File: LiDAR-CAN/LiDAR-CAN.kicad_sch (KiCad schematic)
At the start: 0 parts

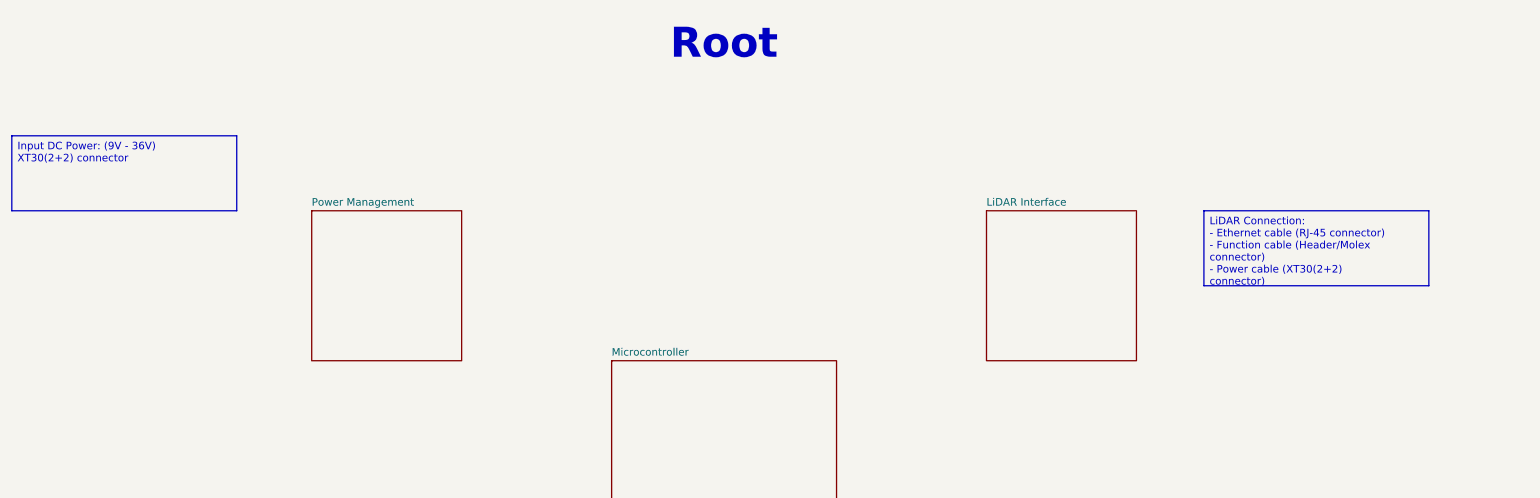
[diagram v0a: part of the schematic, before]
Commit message: Add LiDAR Interface complete circuit
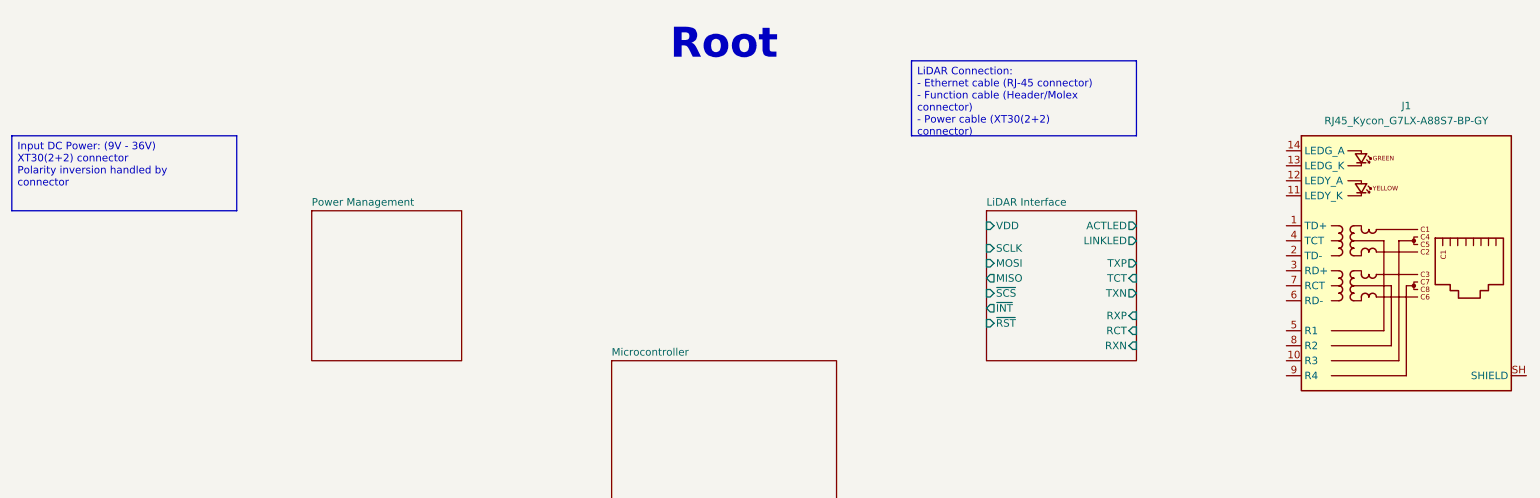
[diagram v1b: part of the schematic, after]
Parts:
- added J1: RJ45_Kycon_G7LX-A88S7-BP-GY, Connector_RJ:RJ45_Kycon_G7LX-A88S7-BP-xx_Horizontal, symbol Connector:RJ45_Kycon_G7LX-A88S7-BP-GY
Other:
- sheet LiDAR Interface ports: added ACTLED, LINKLED, MISO, MOSI, RCT, RXN, RXP, SCLK, TCT, TXN, TXP, VDD, ~{INT}, ~{RST}, ~{SCS}; removed none
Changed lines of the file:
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@@
 	(text_box "LiDAR Connection:\n- Ethernet cable (RJ-45 connector)\n- Function cable (Header/Molex connector)\n- Power cable (XT30(2+2) connector)"
 		(exclude_from_sim no)
-		(at 227.33 50.8 0)
+		(at 177.8 25.4 0)
 		(size 38.1 12.7)
 		(margins 0.9525 0.9525 0.9525 0.9525)
@@
 		)
 	)
-	(text_box "Input DC Power: (9V - 36V)\nXT30(2+2) connector"
+	(text_box "Input DC Power: (9V - 36V)\nXT30(2+2) connector\nPolarity inversion handled by connector"
 		(exclude_from_sim no)
 		(at 25.4 38.1 0)
@@
 		)
 	)
-	(sheet
-		(at 127 76.2)
-		(size 38.1 38.1)
+	(symbol
+		(lib_id "Connector:RJ45_Kycon_G7LX-A88S7-BP-GY")
+		(at 261.62 60.96 0)
+		(unit 1)
 		(exclude_from_sim no)
 		(in_bom yes)
@@
 		(dnp no)
 		(fields_autoplaced yes)
+		(property "Reference" "J1"
+			(at 261.62 33.02 0)
+			(effects
+				(font
+					(size 1.27 1.27)
+				)
+			)
+		)
+		(property "Value" "RJ45_Kycon_G7LX-A88S7-BP-GY"
+			(at 261.62 35.56 0)
+			(effects
+				(font
+					(size 1.27 1.27)
+				)
+			)
+		)
+		(property "Footprint" "Connector_RJ:RJ45_Kycon_G7LX-A88S7-BP-xx_Horizontal"
+			(at 261.62 33.02 0)
+			(effects
+				(font
+					(size 1.27 1.27)
+				)
+				(hide yes)
+			)
+		)
+		(property "Datasheet" "http://www.kycon.com/Pub_Eng_Draw/G7LX-A88S7-BP-GY.pdf"
+			(at 261.62 30.48 0)
+			(effects
+				(font
+					(size 1.27 1.27)
+				)
+				(hide yes)
+			)
+		)
+		(property "Description" "1 Port RJ45 Magjack Connector Through Hole 10/100 Base-T, AutoMDIX"
+			(at 261.62 60.96 0)
+			(effects
+				(font
+					(size 1.27 1.27)
+				)
+				(hide yes)
+			)
+		)
+		(pin "12"
+		)
+		(pin "2"
+		)
+		(pin "SH"
+		)
+		(pin "8"
+		)
+		(pin "6"
+		)
+		(pin "11"
+		)
+		(pin "9"
+		)
+		(pin "13"
+		)
+		(pin "5"
+		)
+		(pin "1"
+		)
+		(pin "14"
+		)
+		(pin "4"
+		)
+		(pin "3"
+		)
+		(pin "7"
+		)
+		(pin "10"
+		)
+		(instances
+			(project ""
+				(path "/56db6f21-0e4a-4321-bd8a-db37f1842dd9"
+					(reference "J1")
+					(unit 1)
+				)
+			)
+		)
+	)
+	(sheet
+		(at 127 76.2)
+		(size 38.1 38.1)
+		(exclude_from_sim no)
+		(in_bom yes)
+		(on_board yes)
+		(dnp no)
+		(fields_autoplaced yes)
 		(stroke
 			(width 0.1524)
@@
 			)
 		)
+		(pin "ACTLED" output
+			(at 215.9 53.34 0)
+			(effects
+				(font
+					(size 1.27 1.27)
+				)
+				(justify right)
+			)
+		)
+		(pin "LINKLED" output
+			(at 215.9 55.88 0)
+			(effects
+				(font
+					(size 1.27 1.27)
+				)
+				(justify right)
+			)
+		)
+		(pin "MISO" output
+			(at 190.5 62.23 180)
+			(effects
+				(font
+					(size 1.27 1.27)
+				)
+				(justify left)
+			)
+		)
+		(pin "MOSI" input
+			(at 190.5 59.69 180)
+			(effects
+				(font
+					(size 1.27 1.27)
+				)
+				(justify left)
+			)
+		)
+		(pin "RCT" input
+			(at 215.9 71.12 0)
+			(effects
+				(font
+					(size 1.27 1.27)
+				)
+				(justify right)
+			)
+		)
+		(pin "RXN" input
+			(at 215.9 73.66 0)
+			(effects
+				(font
+					(size 1.27 1.27)
+				)
+				(justify right)
+			)
+		)
+		(pin "RXP" input
+			(at 215.9 68.58 0)
+			(effects
+				(font
+					(size 1.27 1.27)
+				)
+				(justify right)
+			)
+		)
+		(pin "SCLK" input
+			(at 190.5 57.15 180)
+			(effects
+				(font
+					(size 1.27 1.27)
+				)
+				(justify left)
+			)
+		)
+		(pin "TCT" input
+			(at 215.9 62.23 0)
+			(effects
+				(font
+					(size 1.27 1.27)
+				)
+				(justify right)
+			)
+		)
+		(pin "TXN" output
+			(at 215.9 64.77 0)
+			(effects
+				(font
+					(size 1.27 1.27)
+				)
+				(justify right)
+			)
+		)
+		(pin "TXP" output
+			(at 215.9 59.69 0)
+			(effects
+				(font
+					(size 1.27 1.27)
+				)
+				(justify right)
+			)
+		)
+		(pin "VDD" input
+			(at 190.5 53.34 180)
+			(effects
+				(font
+					(size 1.27 1.27)
+				)
+				(justify left)
+			)
+		)
+		(pin "~{INT}" output
+			(at 190.5 67.31 180)
+			(effects
+				(font
+					(size 1.27 1.27)
+				)
+				(justify left)
+			)
+		)
+		(pin "~{RST}" input
+			(at 190.5 69.85 180)
+			(effects
+				(font
+					(size 1.27 1.27)
+				)
+				(justify left)
+			)
+		)
+		(pin "~{SCS}" input
+			(at 190.5 64.77 180)
+			(effects
+				(font
+					(size 1.27 1.27)
+				)
+				(justify left)
+			)
+		)

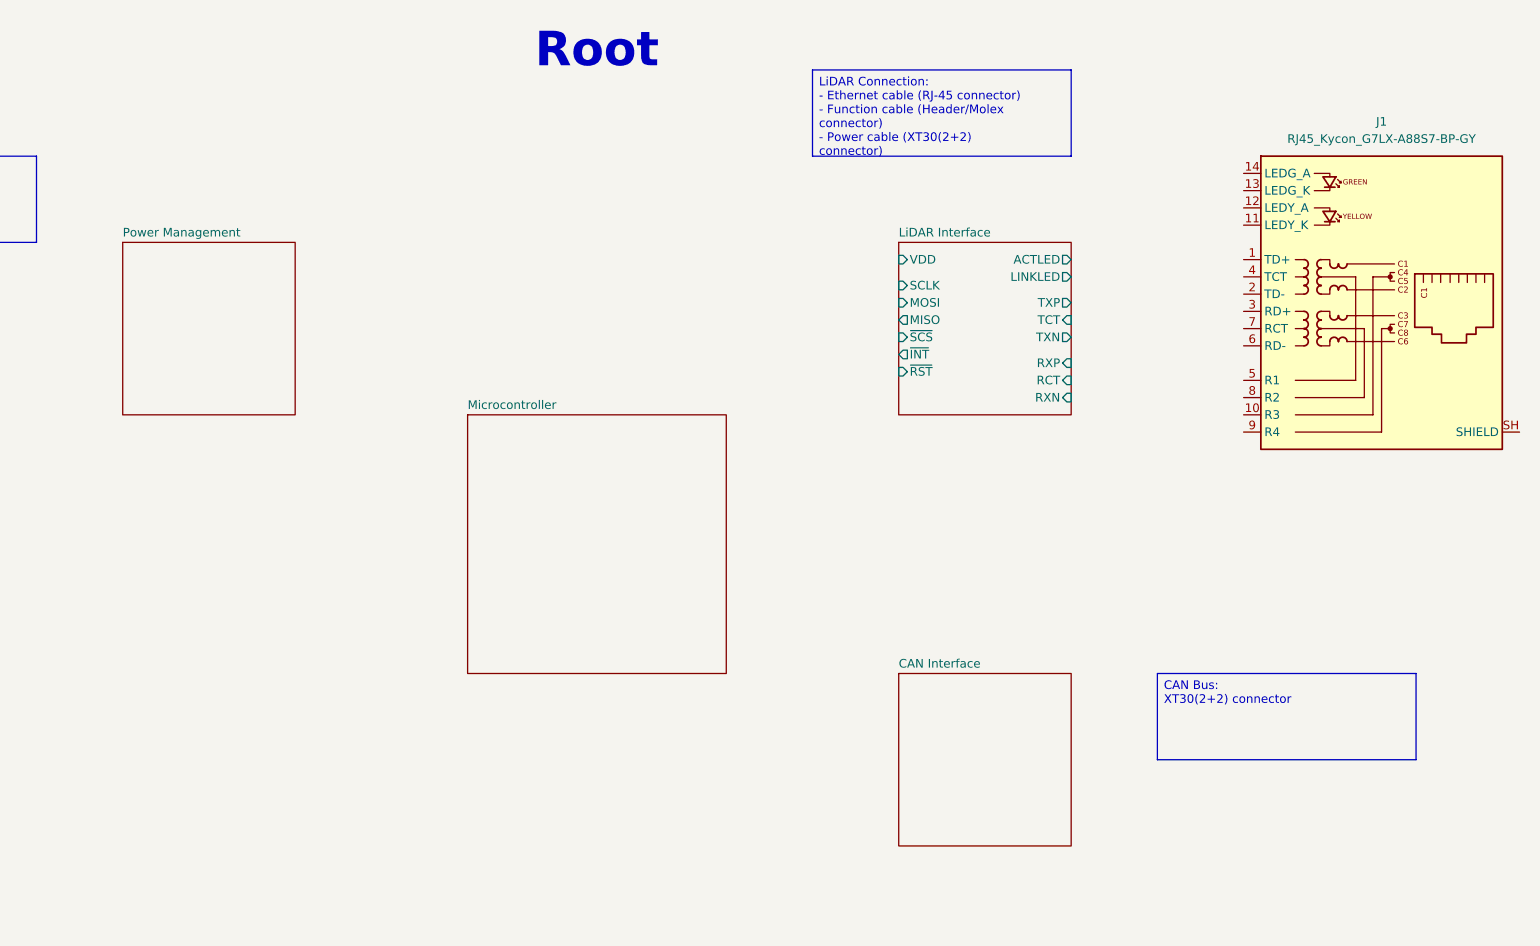
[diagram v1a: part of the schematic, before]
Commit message: Add RJ45 connector circuit
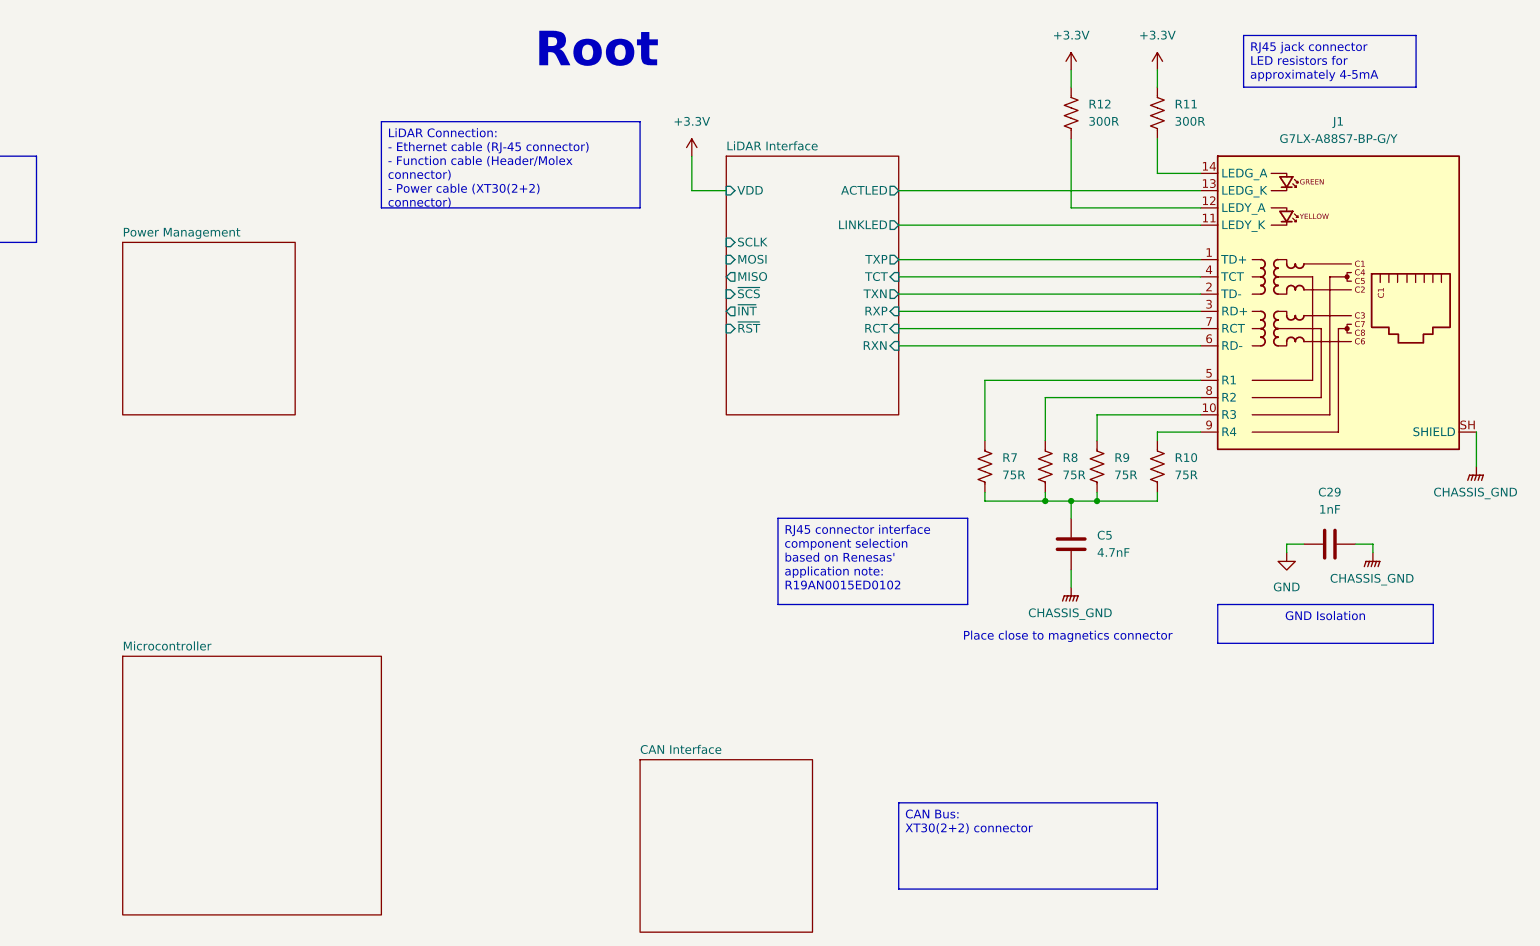
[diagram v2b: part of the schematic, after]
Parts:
- added C29: 1nF, 1000 pF ±20% 2000V (2kV) Ceramic Capacitor X7R 1808 (4520 Metric), symbol Device:C
- added C5: 4.7nF, Capacitor_SMD:C_0603_1608Metric, symbol Device:C
- added R10, R7, R8, R9: 75R, Resistor_SMD:R_0603_1608Metric, symbol Device:R_US
- added R11, R12: 300R, Resistor_SMD:R_0603_1608Metric, symbol Device:R_US
- J1: value RJ45_Kycon_G7LX-A88S7-BP-GY -> G7LX-A88S7-BP-G/Y; MPN (none) -> G7LX-A88S7-BP-G/Y; Manufacturer (none) -> Kycon, Inc.
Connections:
- net LiDAR Interface/ACTLED: now also J1.13 (LEDG_K)
- net LiDAR Interface/LINKLED: now also J1.11 (LEDY_K)
- net LiDAR Interface/RCT: now also J1.7 (RCT)
- net LiDAR Interface/RXN: now also J1.6 (RD-)
- net LiDAR Interface/RXP: now also J1.3 (RD+)
- net LiDAR Interface/TCT: now also J1.4 (TCT)
- net LiDAR Interface/TXN: now also J1.2 (TD-)
- net LiDAR Interface/TXP: now also J1.1 (TD+)
- net at J1.10 (R3): now also R9.1
- net at J1.12 (LEDY_A): now also R12.2
- net at J1.14 (LEDG_A): now also R11.2
- net at J1.5 (R1): now also R7.1
- net at J1.8 (R2): now also R8.1
- net at J1.9 (R4): now also R10.1
- net CHASSIS_GND: now reaches J1.SH (SHIELD)
- net CHASSIS_GND: now also C29.2, C5.2
- new net: C5.1, R10.2, R7.2, R8.2, R9.2
- new net +3.3V: R11.1, R12.1
- new net GND: C29.1
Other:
- note added: "Place close to magnetics connector"
- moved on the sheet: J1

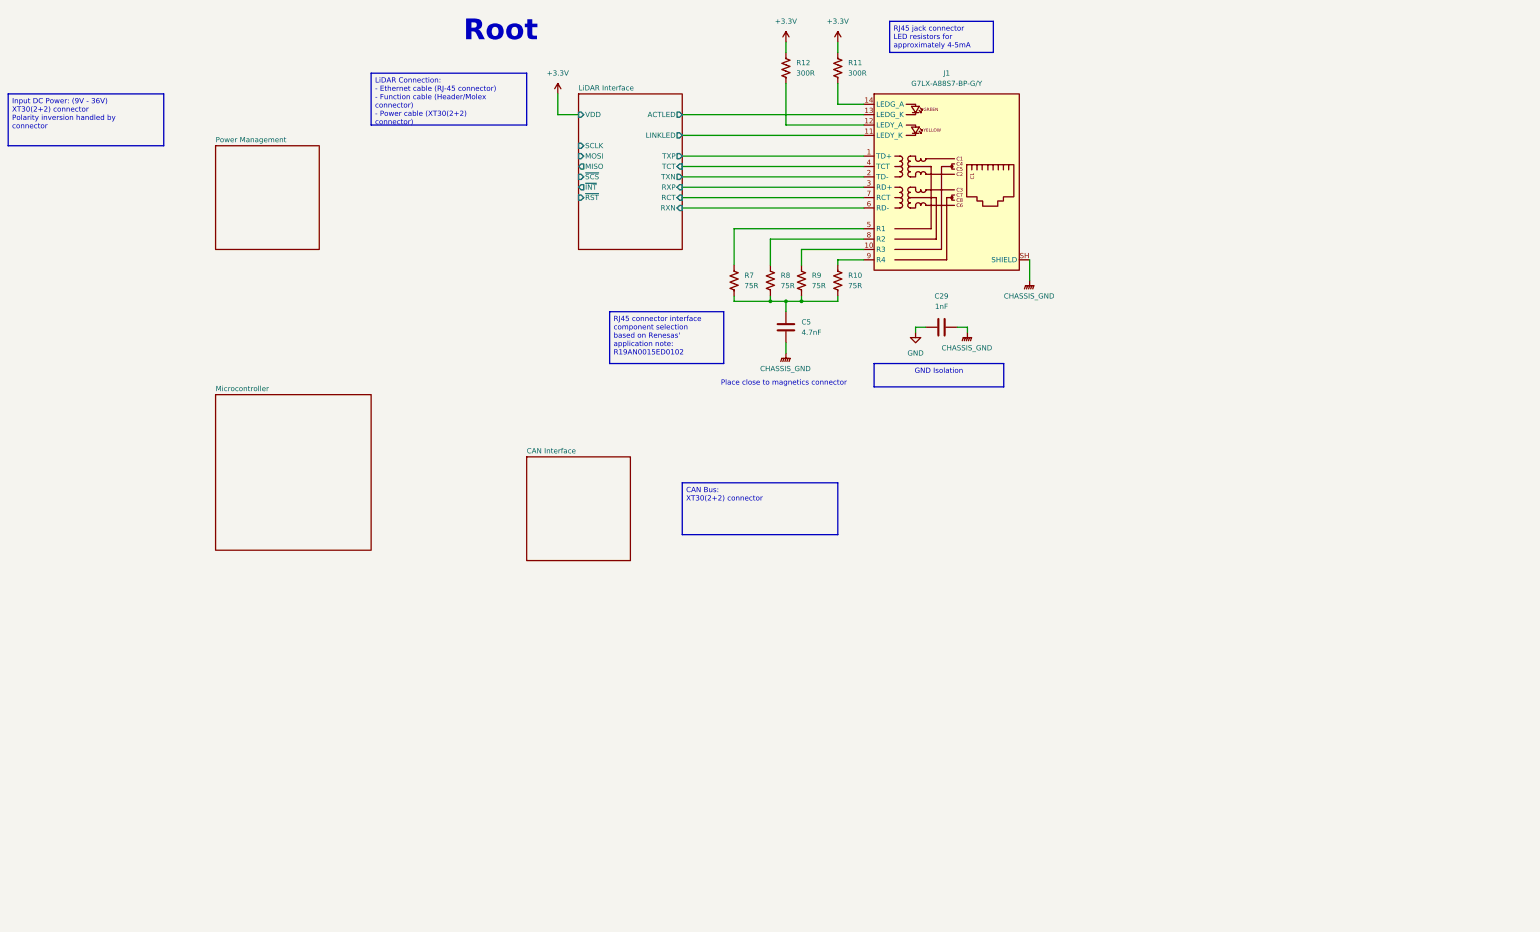
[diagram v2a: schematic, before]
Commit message: Add external connector circuit
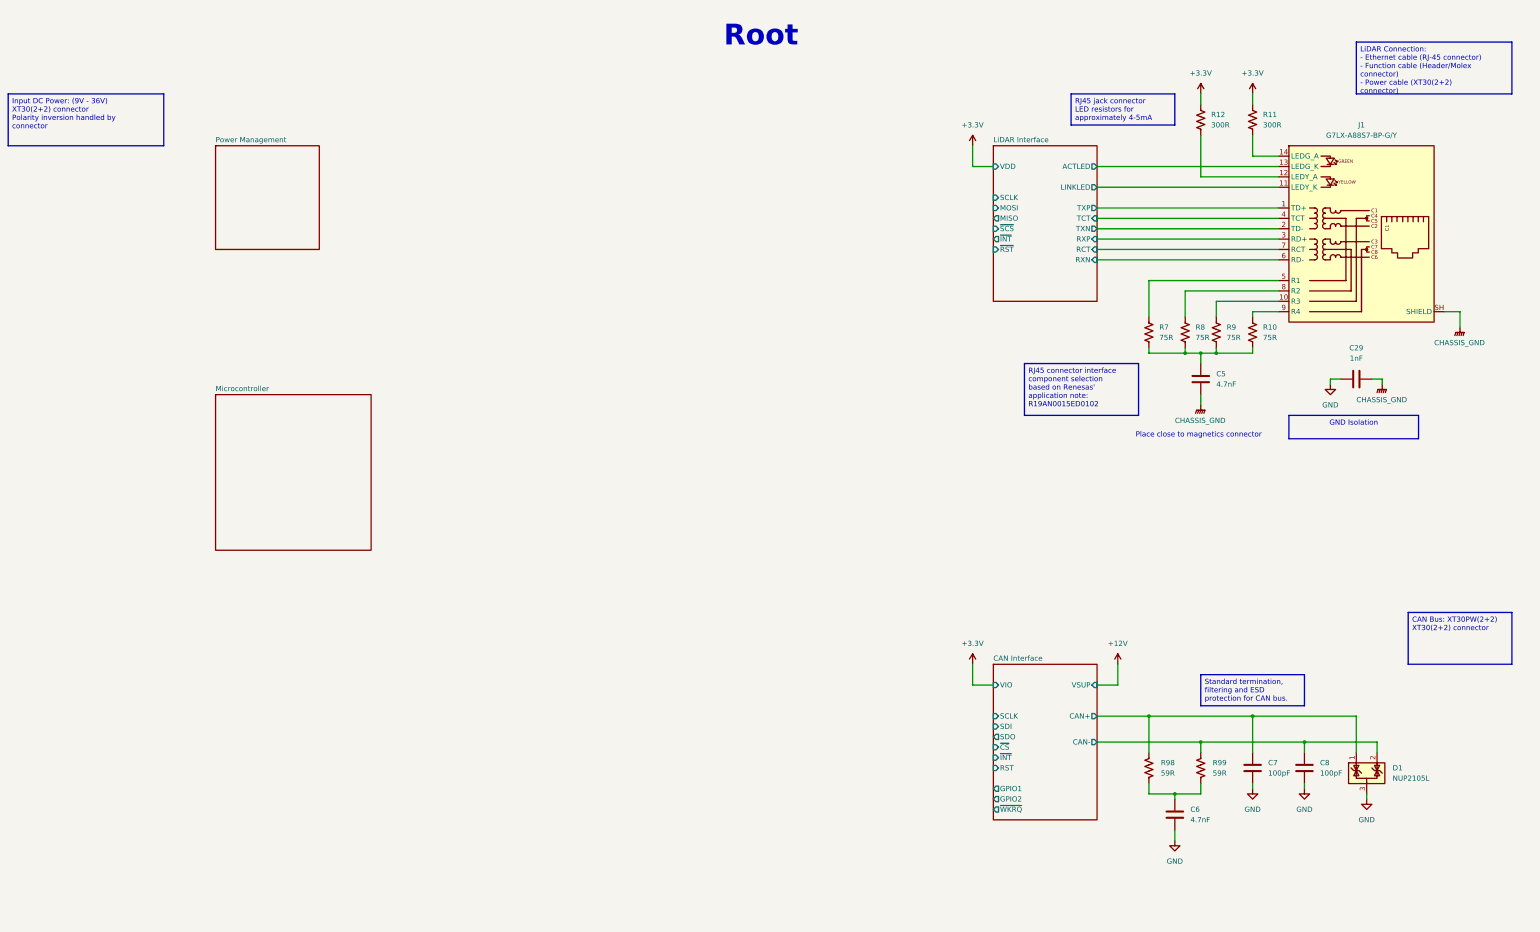
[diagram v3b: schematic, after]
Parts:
- added C6: 4.7nF, Capacitor_SMD:C_0603_1608Metric, symbol Device:C
- added C7, C8: 100pF, Capacitor_SMD:C_0603_1608Metric, symbol Device:C
- added D1: NUP2105L, Package_TO_SOT_SMD:SOT-23, symbol Power_Protection:NUP2105L
- added R98, R99: 59R, Resistor_SMD:R_0603_1608Metric, symbol Symbols:RES 1.2K OHM 5% 1/10W 0603
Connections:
- net GND: now also C6.2, C7.2, C8.2, D1.3 (A)
- new net: C6.1, R98.1, R99.1
- new net CAN Interface/CAN+: C7.1, D1.1 (K), R98.2
- new net CAN Interface/CAN-: C8.1, D1.2 (K), R99.2
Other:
- sheet CAN Interface ports: added CAN+, CAN-, GPIO1, GPIO2, RST, SCLK, SDI, SDO, VIO, VSUP, ~{CS}, ~{INT}, ~{WKRQ}; removed none
- moved on the sheet: C29, C5, J1, R10, R11, R12, R7, R8, R9

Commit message: Add complete MCU circuit
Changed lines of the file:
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@@
 		)
 		(pin "~{INT}" output
-			(at 266.7 73.66 180)
+			(at 266.7 76.2 180)
 			(effects
 				(font
@@
 		)
 		(pin "~{RST}" input
-			(at 266.7 76.2 180)
+			(at 266.7 78.74 180)
 			(effects
 				(font
@@
 		)
 		(pin "RST" input
-			(at 266.7 203.2 180)
+			(at 266.7 205.74 180)
 			(effects
 				(font
@@
 		)
 		(pin "~{INT}" input
-			(at 266.7 200.66 180)
+			(at 266.7 203.2 180)
 			(effects
 				(font
